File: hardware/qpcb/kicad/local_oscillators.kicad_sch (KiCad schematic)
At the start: 11 parts, among them Y1 SiT5157AI-FK-33N0-100.000000X

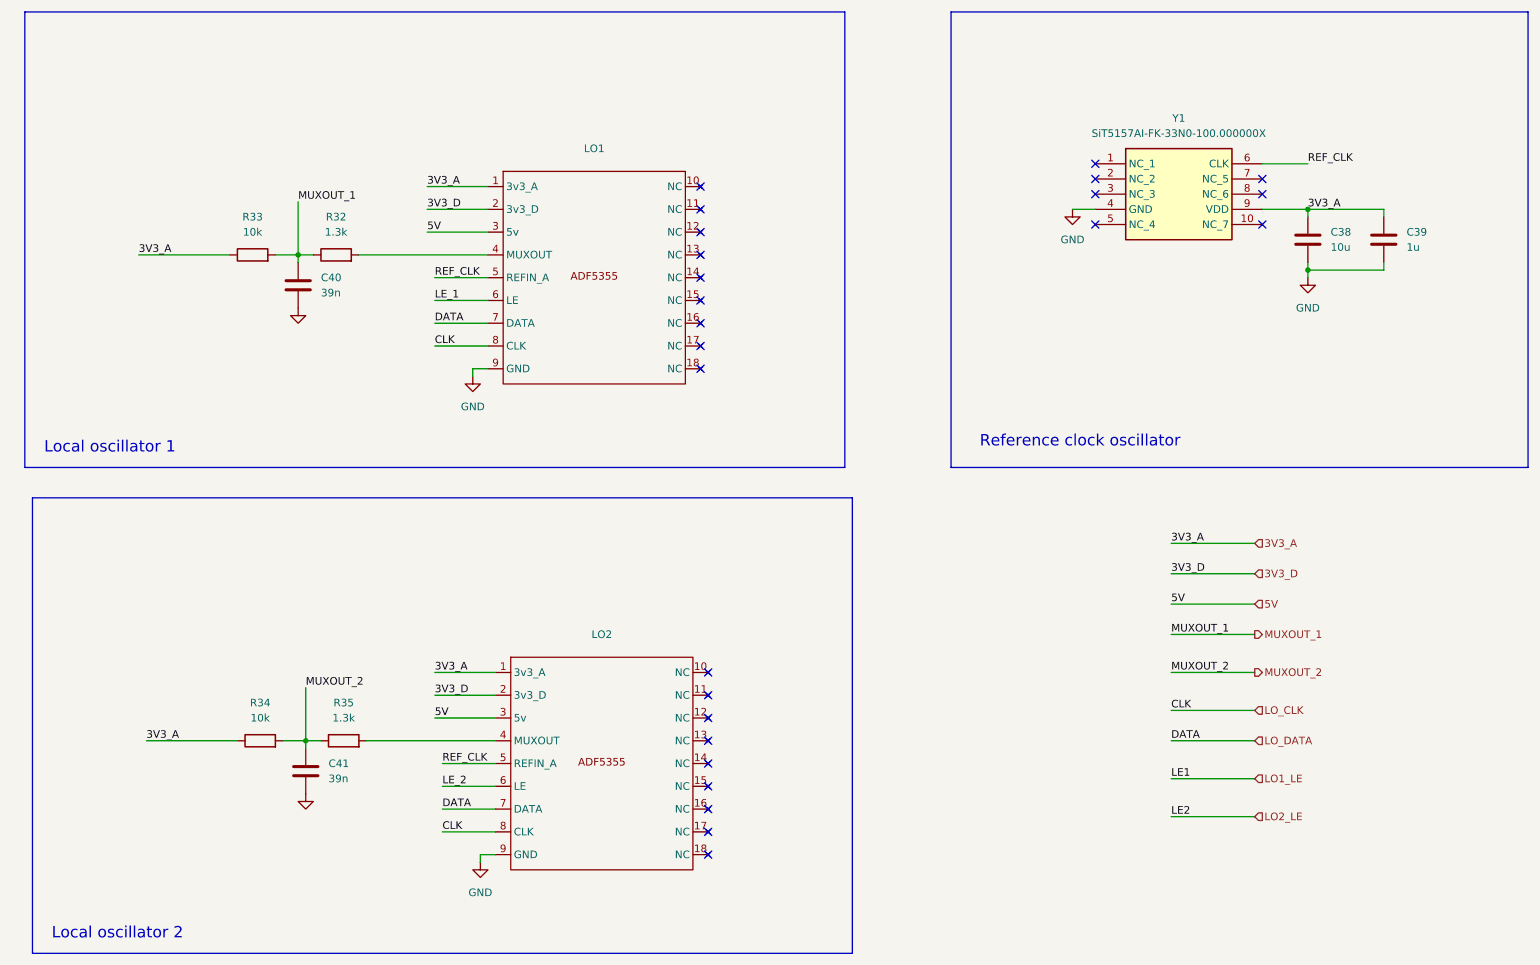
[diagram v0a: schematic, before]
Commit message: Complete PSU simulations and fix ERC errors
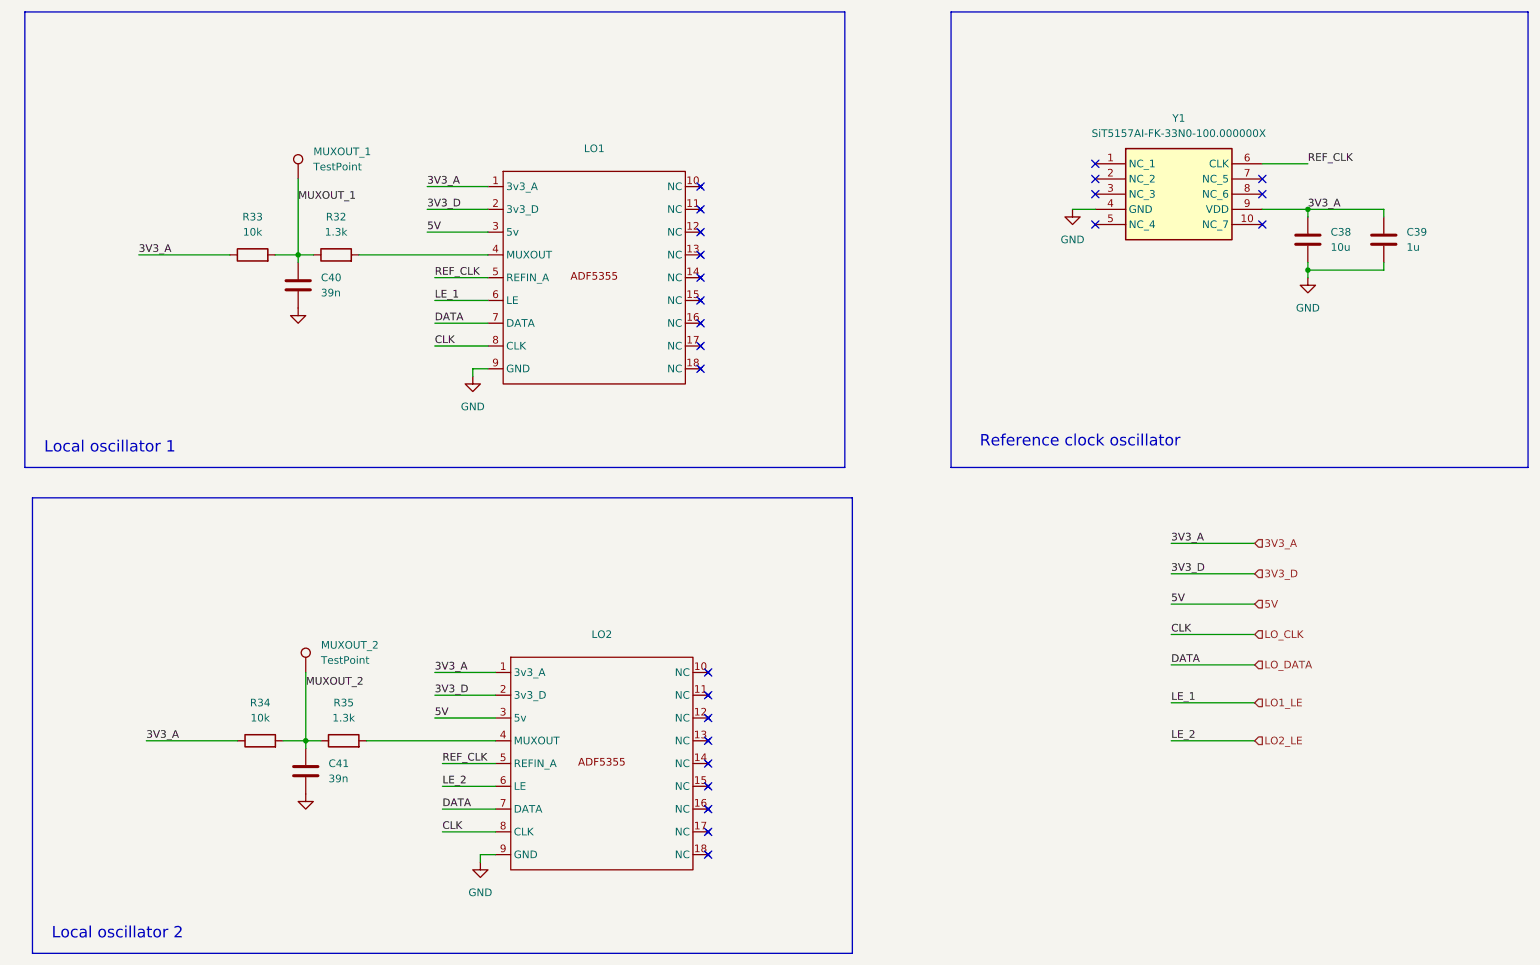
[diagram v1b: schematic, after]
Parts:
- added MUXOUT_1, MUXOUT_2: TestPoint, symbol Connector:TestPoint
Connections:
- net LE_1 is gone; now on net LO1_LE: LO1.6 (LE)
- net LE_2 is gone; now on net LO2_LE: LO2.6 (LE)
- net MUXOUT_1: now also MUXOUT_1.1
- net MUXOUT_2: now also MUXOUT_2.1

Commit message: Final version of MC43063A and fill components' production info
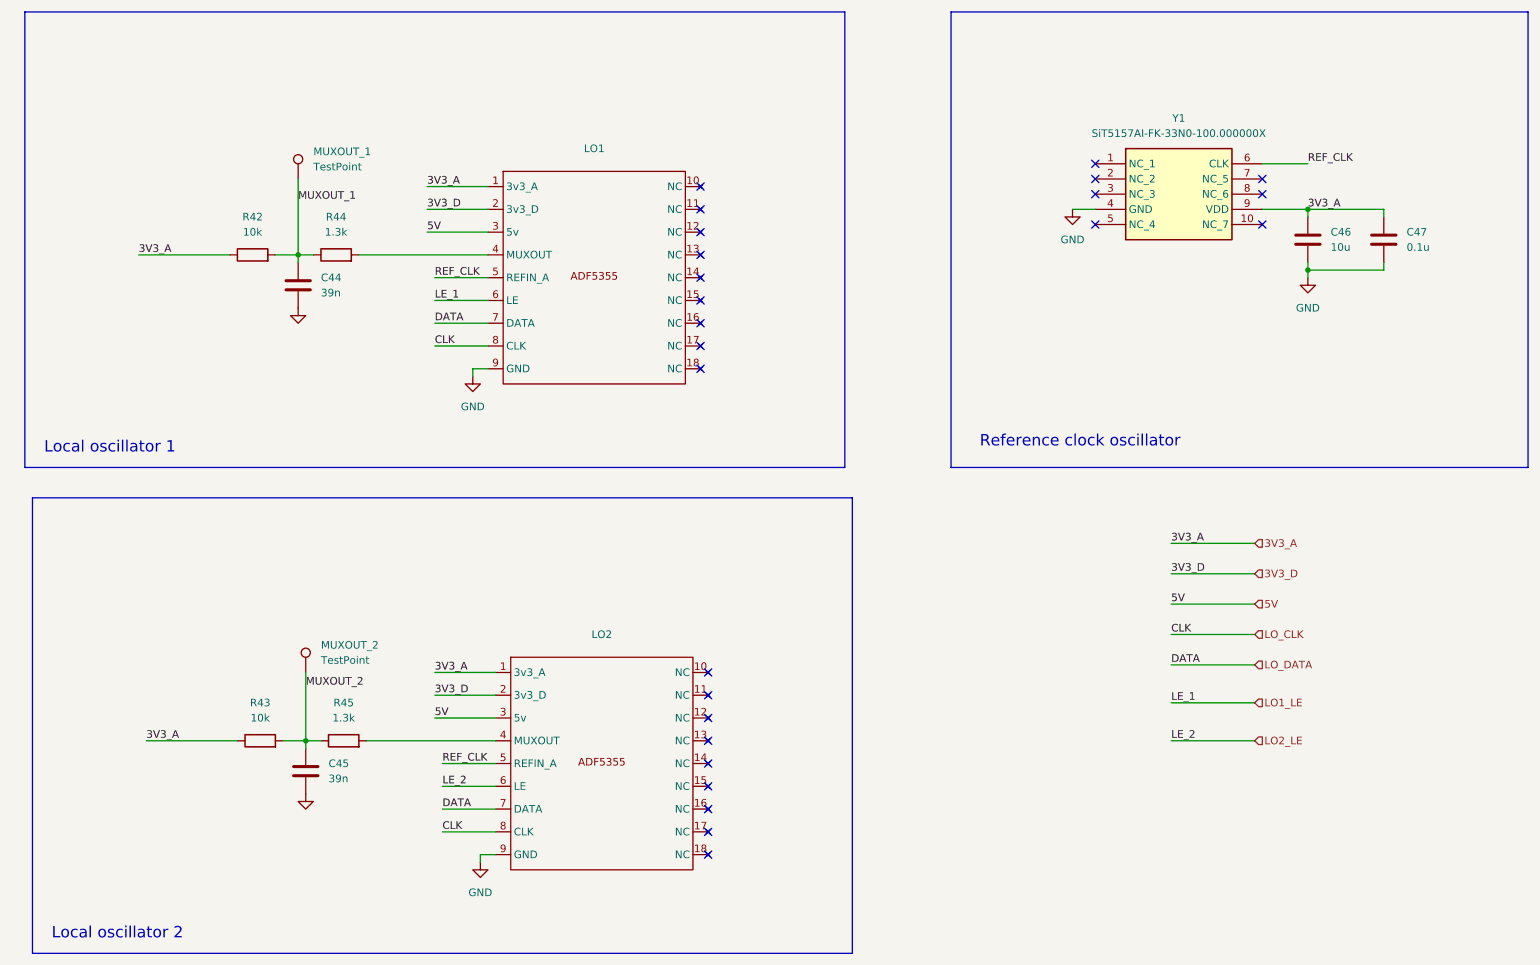
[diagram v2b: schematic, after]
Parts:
- C47: renamed from C39; value 1u -> 0.1u
- Y1: footprint SiT5157AIFK33N0100000000X -> footprints:SiT5157AIFK33N0100000000X; Manufacturer (none) -> SiTime; Manufacturer Part Number (none) -> SiT5157AI-FK-33N0-100.000000X; Manufacturer_Name SiTime -> (none); Manufacturer_Part_Number SiT5157AI-FK-33N0-100.000000X -> (none); Package (none) -> CQFN-10
- renumbered C40 to C44, C41 to C45, C38 to C46, R33 to R42, R34 to R43, R32 to R44, R35 to R45

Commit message: Add footprints and 3d CAD models of components
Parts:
- C44, C45: footprint Capacitor_SMD:C_0402_1005Metric_Pad0.74x0.62mm_HandSolder -> Capacitor_SMD:C_0805_2012Metric_Pad1.18x1.45mm_HandSolder; Manufacturer (none) -> Vishay; Manufacturer Part Number (none) -> VJ0805Y393KXJAC; Mouser Part Number (none) -> 77-VJ0805Y393KXJAC; Mouser Price/Stock (none) -> https://www.mouser.it/ProductDetail/Vishay-Vitramon/VJ0805Y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; Package (none) -> 0805
- C46: footprint (none) -> Capacitor_SMD:C_0805_2012Metric_Pad1.18x1.45mm_HandSolder
- C47: footprint (none) -> Capacitor_SMD:C_0805_2012Metric_Pad1.18x1.45mm_HandSolder; Manufacturer (none) -> KYOCERA AVX; Manufacturer Part Number (none) -> 08053C104JAZ2A; Mouser Part Number (none) -> 581-08053C104JAZ2A; Mouser Price/Stock (none) -> https://www.mouser.it/ProductDetail/KYOCERA-AVX/08053C104JA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; Package (none) -> 0805
- R42, R43: footprint Resistor_SMD:R_0402_1005Metric_Pad0.72x0.64mm_HandSolder -> Capacitor_SMD:C_0805_2012Metric_Pad1.18x1.45mm_HandSolder
- R44, R45: footprint Resistor_SMD:R_0402_1005Metric_Pad0.72x0.64mm_HandSolder -> Capacitor_SMD:C_0805_2012Metric_Pad1.18x1.45mm_HandSolder; Manufacturer (none) -> Panasonic; Manufacturer Part Number (none) -> ERJ-S06F1301V; Mouser Part Number (none) -> 667-ERJ-S06F1301V; Mouser Price/Stock (none) -> https://www.mouser.it/ProductDetail/Panasonic/ERJ-S06F1301V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; Package (none) -> 0805

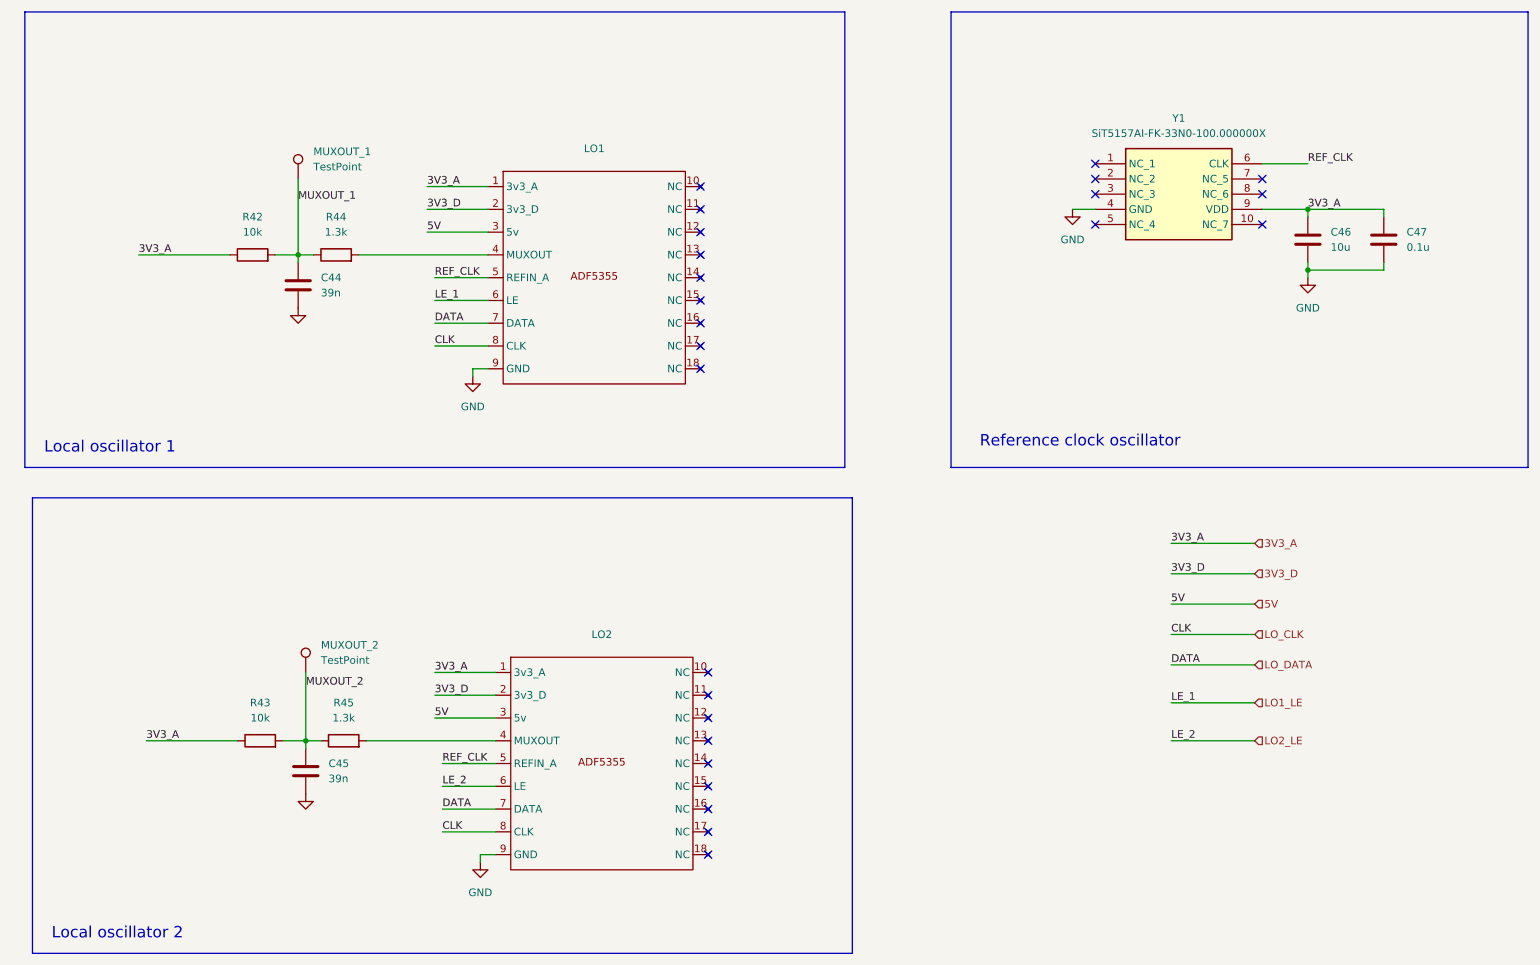
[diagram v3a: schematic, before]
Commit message: Add final footprints of daughter boards, change components for -3v3 power supply line and placement almost finished
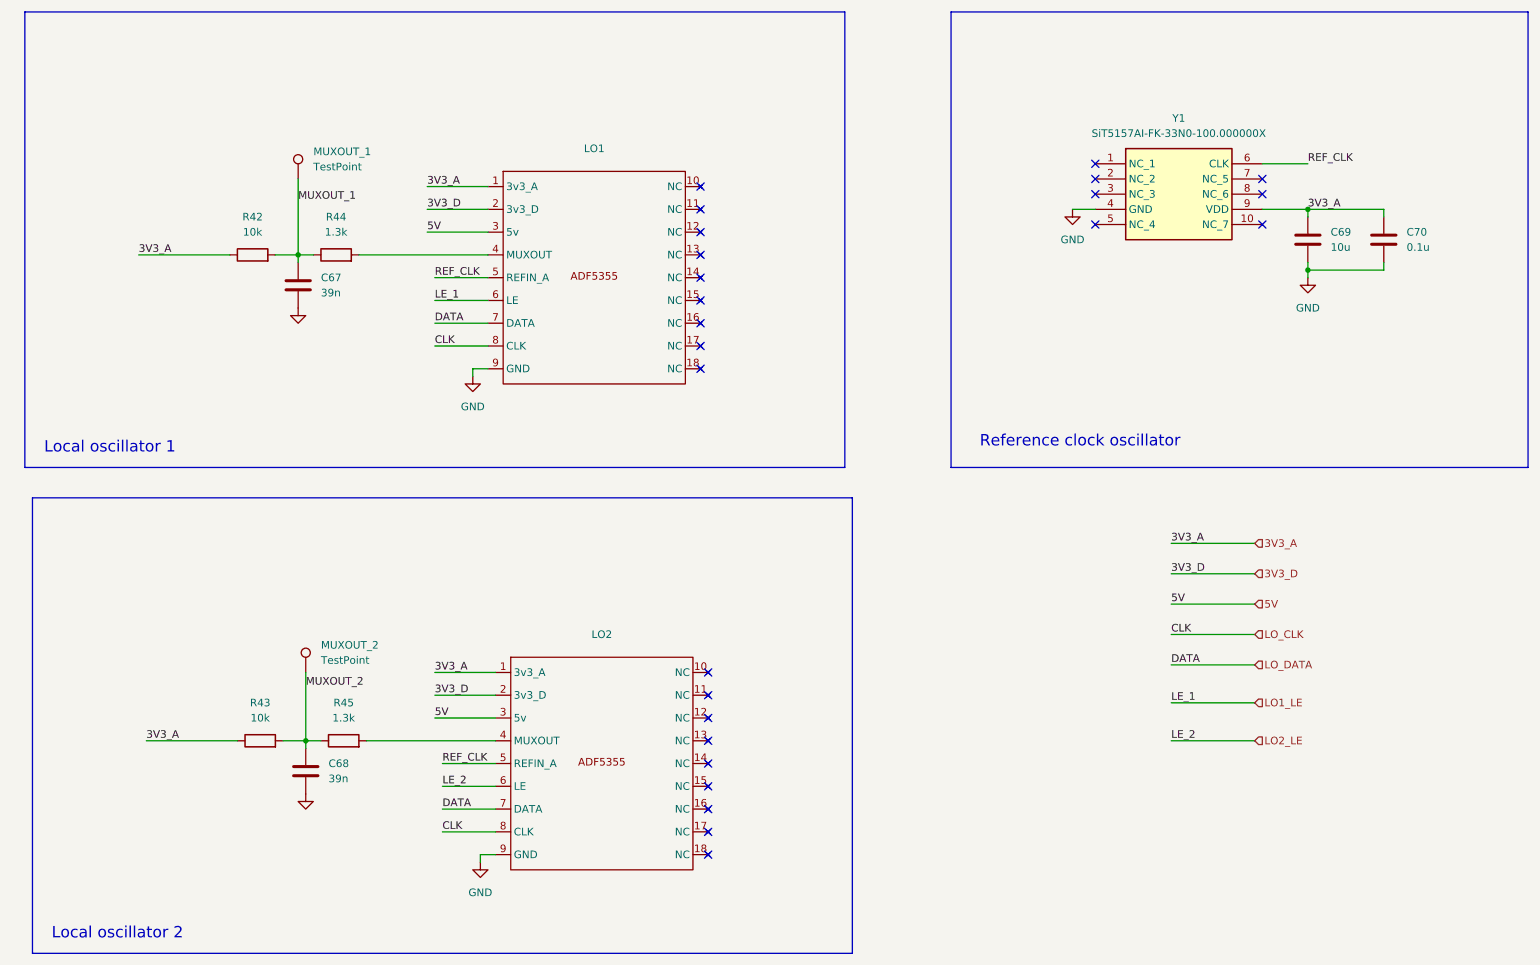
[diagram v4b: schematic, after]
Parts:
- LO1, LO2: footprint (none) -> footprints:LO
- MUXOUT_1, MUXOUT_2: footprint (none) -> TestPoint:TestPoint_Pad_D1.5mm
- renumbered C44 to C67, C45 to C68, C46 to C69, C47 to C70
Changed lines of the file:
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@@
 		(dnp no)
 		(fields_autoplaced yes)
-		(property "Reference" "C46"
+		(property "Reference" "C69"
 			(at 236.22 57.1499 0)
 			(effects
@@
 			(project "qpcb"
 				(path "/c131d68b-62f5-4c45-b130-1d10920b3403/b685e560-a45a-4313-8d29-a96968b46a78"
-					(reference "C46")
+					(reference "C69")
 					(unit 1)
 				)
@@
 		(dnp no)
 		(fields_autoplaced yes)
-		(property "Reference" "#PWR080"
+		(property "Reference" "#PWR0105"
 			(at 63.5 76.2 0)
 			(effects
@@
 			(project "qpcb"
 				(path "/c131d68b-62f5-4c45-b130-1d10920b3403/b685e560-a45a-4313-8d29-a96968b46a78"
-					(reference "#PWR080")
+					(reference "#PWR0105")
 					(unit 1)
 				)
@@
 		(dnp no)
 		(fields_autoplaced yes)
-		(property "Reference" "#PWR081"
+		(property "Reference" "#PWR0106"
 			(at 64.77 157.48 0)
 			(effects
@@
 			(project "qpcb"
 				(path "/c131d68b-62f5-4c45-b130-1d10920b3403/b685e560-a45a-4313-8d29-a96968b46a78"
-					(reference "#PWR081")
+					(reference "#PWR0106")
 					(unit 1)
 				)
@@
 		(dnp no)
 		(fields_autoplaced yes)
-		(property "Reference" "C45"
+		(property "Reference" "C68"
 			(at 68.58 146.0499 0)
 			(effects
@@
 			(project "qpcb"
 				(path "/c131d68b-62f5-4c45-b130-1d10920b3403/b685e560-a45a-4313-8d29-a96968b46a78"
-					(reference "C45")
+					(reference "C68")
 					(unit 1)
 				)
@@
 		(dnp no)
 		(fields_autoplaced yes)
-		(property "Reference" "#PWR084"
+		(property "Reference" "#PWR0109"
 			(at 193.04 59.69 0)
 			(effects
@@
 			(project "qpcb"
 				(path "/c131d68b-62f5-4c45-b130-1d10920b3403/b685e560-a45a-4313-8d29-a96968b46a78"
-					(reference "#PWR084")
+					(reference "#PWR0109")
 					(unit 1)
 				)
@@
 		(dnp no)
 		(fields_autoplaced yes)
-		(property "Reference" "#PWR085"
+		(property "Reference" "#PWR0110"
 			(at 232.41 71.12 0)
 			(effects
@@
 			(project "qpcb"
 				(path "/c131d68b-62f5-4c45-b130-1d10920b3403/b685e560-a45a-4313-8d29-a96968b46a78"
-					(reference "#PWR085")
+					(reference "#PWR0110")
 					(unit 1)
 				)
@@
 		(dnp no)
 		(fields_autoplaced yes)
-		(property "Reference" "#PWR083"
+		(property "Reference" "#PWR0108"
 			(at 93.98 168.91 0)
 			(effects
@@
 			(project "qpcb"
 				(path "/c131d68b-62f5-4c45-b130-1d10920b3403/b685e560-a45a-4313-8d29-a96968b46a78"
-					(reference "#PWR083")
+					(reference "#PWR0108")
 					(unit 1)
 				)
@@
 		(dnp no)
 		(fields_autoplaced yes)
-		(property "Reference" "C44"
+		(property "Reference" "C67"
 			(at 67.31 64.7699 0)
 			(effects
@@
 			(project "qpcb"
 				(path "/c131d68b-62f5-4c45-b130-1d10920b3403/b685e560-a45a-4313-8d29-a96968b46a78"
-					(reference "C44")
+					(reference "C67")
 					(unit 1)
 				)
@@
 		(dnp no)
 		(fields_autoplaced yes)
-		(property "Reference" "C47"
+		(property "Reference" "C70"
 			(at 248.92 57.1499 0)
 			(effects
@@
 			(project "qpcb"
 				(path "/c131d68b-62f5-4c45-b130-1d10920b3403/b685e560-a45a-4313-8d29-a96968b46a78"
-					(reference "C47")
+					(reference "C70")
 					(unit 1)
 				)
@@
 			)
 		)
-		(property "Footprint" ""
+		(property "Footprint" "footprints:LO"
 			(at 113.03 44.45 0)
 			(effects
@@
 			)
 		)
-		(property "Footprint" ""
+		(property "Footprint" "TestPoint:TestPoint_Pad_D1.5mm"
 			(at 69.85 130.81 0)
 			(effects
@@
 			)
 		)
-		(property "Footprint" ""
+		(property "Footprint" "footprints:LO"
 			(at 114.3 125.73 0)
 			(effects
@@
 			)
 		)
-		(property "Footprint" ""
+		(property "Footprint" "TestPoint:TestPoint_Pad_D1.5mm"
 			(at 68.58 48.26 0)
 			(effects
@@
 		(dnp no)
 		(fields_autoplaced yes)
-		(property "Reference" "#PWR082"
+		(property "Reference" "#PWR0107"
 			(at 92.71 87.63 0)
 			(effects
@@
 			(project "qpcb"
 				(path "/c131d68b-62f5-4c45-b130-1d10920b3403/b685e560-a45a-4313-8d29-a96968b46a78"
-					(reference "#PWR082")
+					(reference "#PWR0107")
 					(unit 1)
 				)

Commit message: Add QPCB JLCPCB production files
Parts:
- C67, C68: LCSC (none) -> C3881405
- C70: LCSC (none) -> C2170167
- R44, R45: LCSC (none) -> C2110984
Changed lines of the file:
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@@
+			)
+		)
+		(property "LCSC" "C3881405"
+			(at 64.77 147.32 0)
+			(effects
+				(font
+					(size 1.27 1.27)
+				)
+				(hide yes)
 			)
 		)
@@
 			)
 		)
+		(property "LCSC" "C2110984"
+			(at 69.85 60.96 0)
+			(effects
+				(font
+					(size 1.27 1.27)
+				)
+				(hide yes)
+			)
+		)
 		(pin "1"
 		)
@@
 			)
 		)
+		(property "LCSC" "C2110984"
+			(at 71.12 142.24 0)
+			(effects
+				(font
+					(size 1.27 1.27)
+				)
+				(hide yes)
+			)
+		)
 		(pin "1"
 		)
@@
 			)
 		)
+		(property "LCSC" "C3881405"
+			(at 63.5 66.04 0)
+			(effects
+				(font
+					(size 1.27 1.27)
+				)
+				(hide yes)
+			)
+		)
 		(pin "1"
 		)
@@
 			(at 245.11 58.42 0)
 			(effects
+				(font
+					(size 1.27 1.27)
+				)
+				(hide yes)
+			)
+		)
+		(property "LCSC" "C2170167"
+			(at 245.11 58.42 0)
+			(effects
